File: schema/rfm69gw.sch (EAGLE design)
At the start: 18 parts, among them IC1 ESP-12-SMD, IC2 AMS1117-3.3, J1 POWER_JACKPTH, U1 RFM69CW

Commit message: Board images
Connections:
- net GND: now also X1.GND2, X1.GND4
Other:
- moved on the sheet: C1, C2, C3, C4, FLASH, IC1, IC2, J1, JP1, JP3, R1, R2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

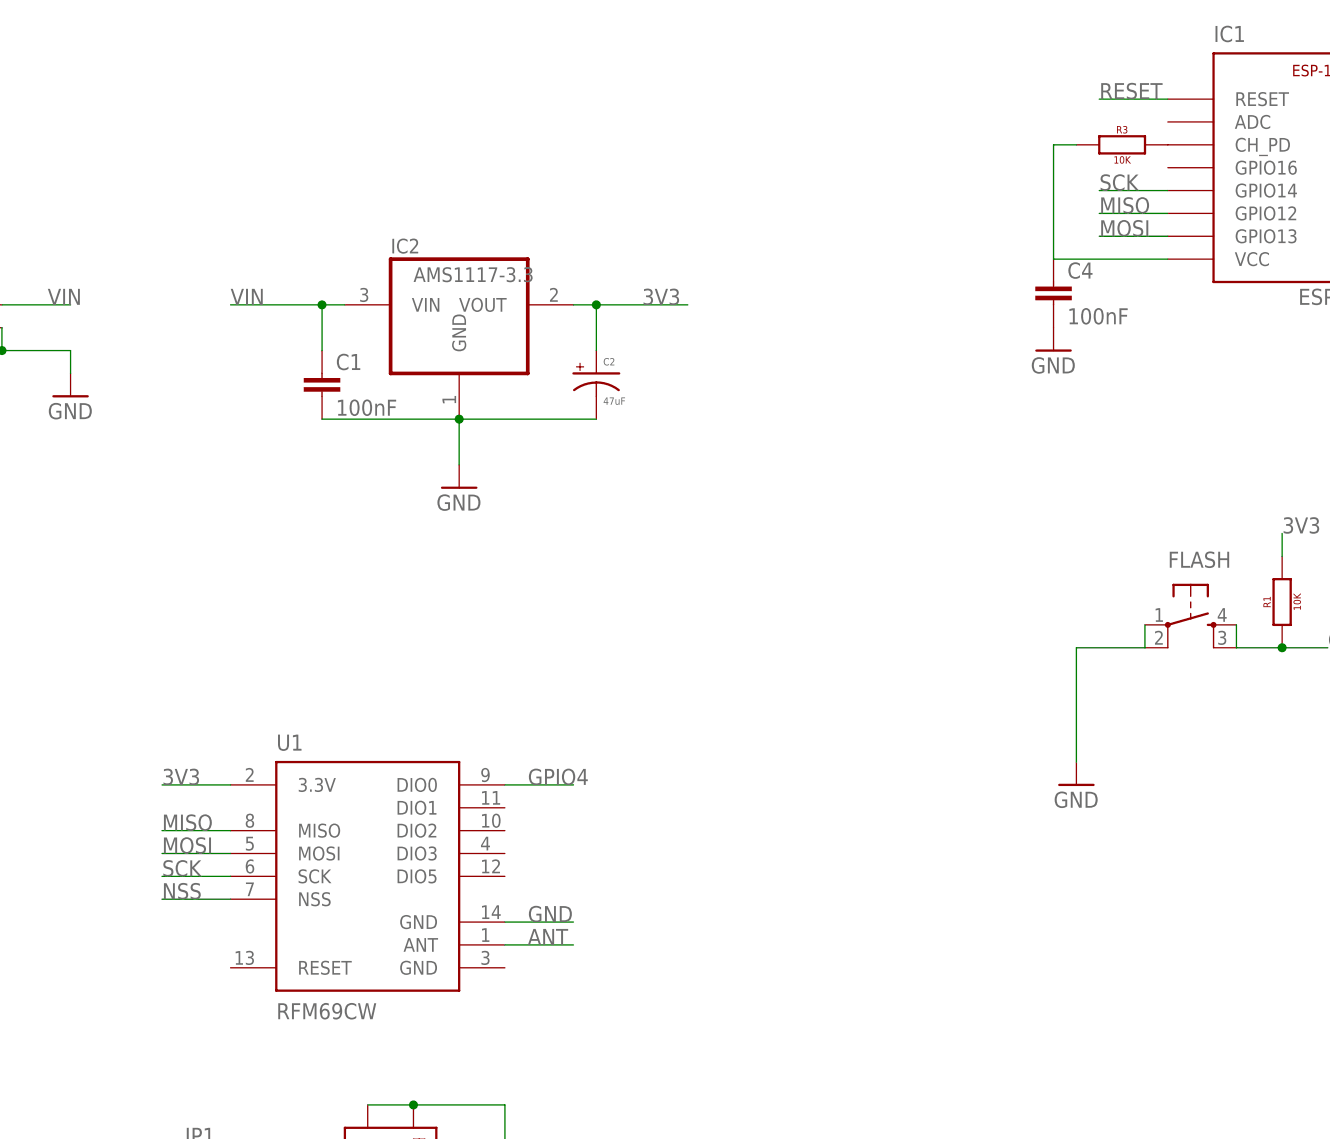
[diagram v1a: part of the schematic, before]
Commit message: Schema updated
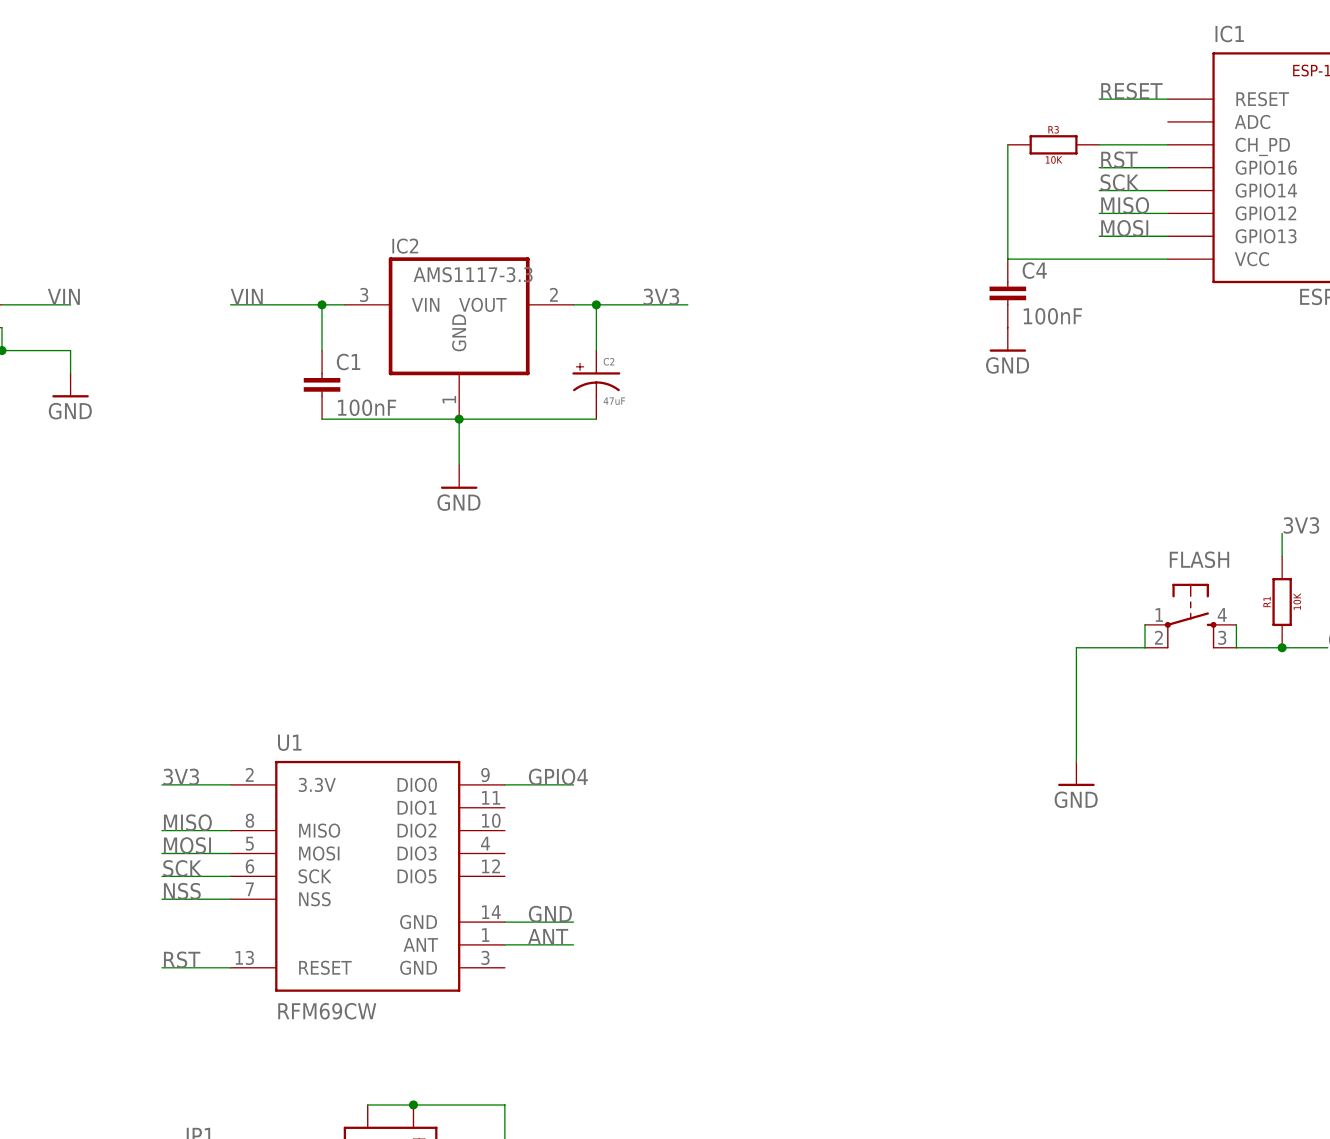
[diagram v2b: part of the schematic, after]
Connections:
- new net RST: IC1.GPIO16, U1.RESET
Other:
- moved on the sheet: C4, R3
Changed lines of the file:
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@@
 <instance part="GND3" gate="1" x="154.94" y="83.82"/>
 <instance part="GND4" gate="1" x="195.58" y="83.82"/>
-<instance part="R3" gate="G$1" x="160.02" y="154.94"/>
+<instance part="R3" gate="G$1" x="152.4" y="154.94"/>
 <instance part="R4" gate="G$1" x="210.82" y="154.94" rot="R270"/>
 <instance part="C3" gate="G$1" x="218.44" y="91.44" rot="R180"/>
 <instance part="R5" gate="G$1" x="236.22" y="154.94" rot="R90"/>
-<instance part="GND7" gate="1" x="152.4" y="132.08"/>
-<instance part="C4" gate="G$1" x="152.4" y="139.7"/>
+<instance part="GND7" gate="1" x="147.32" y="132.08"/>
+<instance part="C4" gate="G$1" x="147.32" y="139.7"/>
 <instance part="IC1" gate="G$1" x="170.18" y="139.7"/>
 <instance part="GND6" gate="1" x="210.82" y="137.16"/>
@@
 <segment>
 <pinref part="R3" gate="G$1" pin="1"/>
-<wire x1="152.4" y1="154.94" x2="154.94" y2="154.94" width="0.1524" layer="91"/>
 <pinref part="C4" gate="G$1" pin="1"/>
-<wire x1="152.4" y1="154.94" x2="152.4" y2="142.24" width="0.1524" layer="91"/>
+<wire x1="147.32" y1="154.94" x2="147.32" y2="142.24" width="0.1524" layer="91"/>
 <pinref part="IC1" gate="G$1" pin="VCC"/>
-<wire x1="165.1" y1="142.24" x2="152.4" y2="142.24" width="0.1524" layer="91"/>
+<wire x1="165.1" y1="142.24" x2="147.32" y2="142.24" width="0.1524" layer="91"/>
 </segment>
 <segment>
@@
 <pinref part="IC1" gate="G$1" pin="CH_PD"/>
 <pinref part="R3" gate="G$1" pin="2"/>
+<wire x1="157.48" y1="154.94" x2="165.1" y2="154.94" width="0.1524" layer="91"/>
 </segment>
 </net>
@@
 </segment>
 </net>
+<net name="RST" class="0">
+<segment>
+<pinref part="U1" gate="G$1" pin="RESET"/>
+<wire x1="60.96" y1="63.5" x2="53.34" y2="63.5" width="0.1524" layer="91"/>
+<label x="53.34" y="63.5" size="1.778" layer="95"/>
+</segment>
+<segment>
+<pinref part="IC1" gate="G$1" pin="GPIO16"/>
+<wire x1="165.1" y1="152.4" x2="157.48" y2="152.4" width="0.1524" layer="91"/>
+<label x="157.48" y="152.4" size="1.778" layer="95"/>
+</segment>
+</net>
